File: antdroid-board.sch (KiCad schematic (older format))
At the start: 55 parts, among them P1 CONN_01X02, Q1 BSS138, Q2 BSS138, U1 LM2678T-5.0, U2 LM2678T-5.0, U3 LM2675M-5

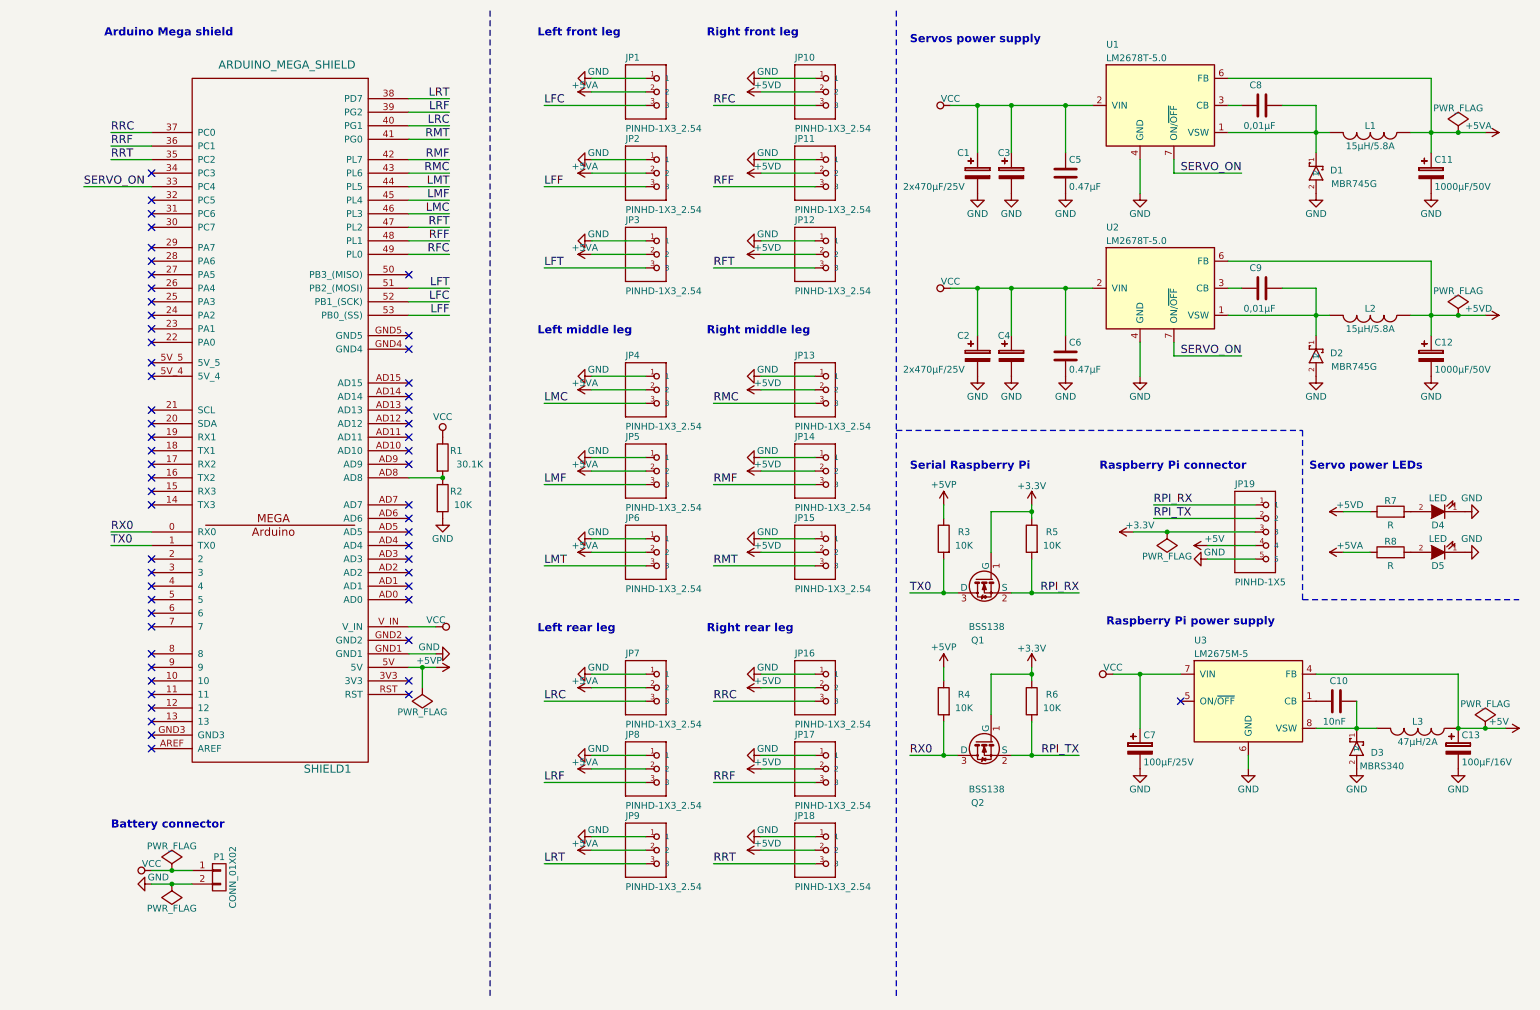
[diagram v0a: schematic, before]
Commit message: All components positioned and design rules almost done
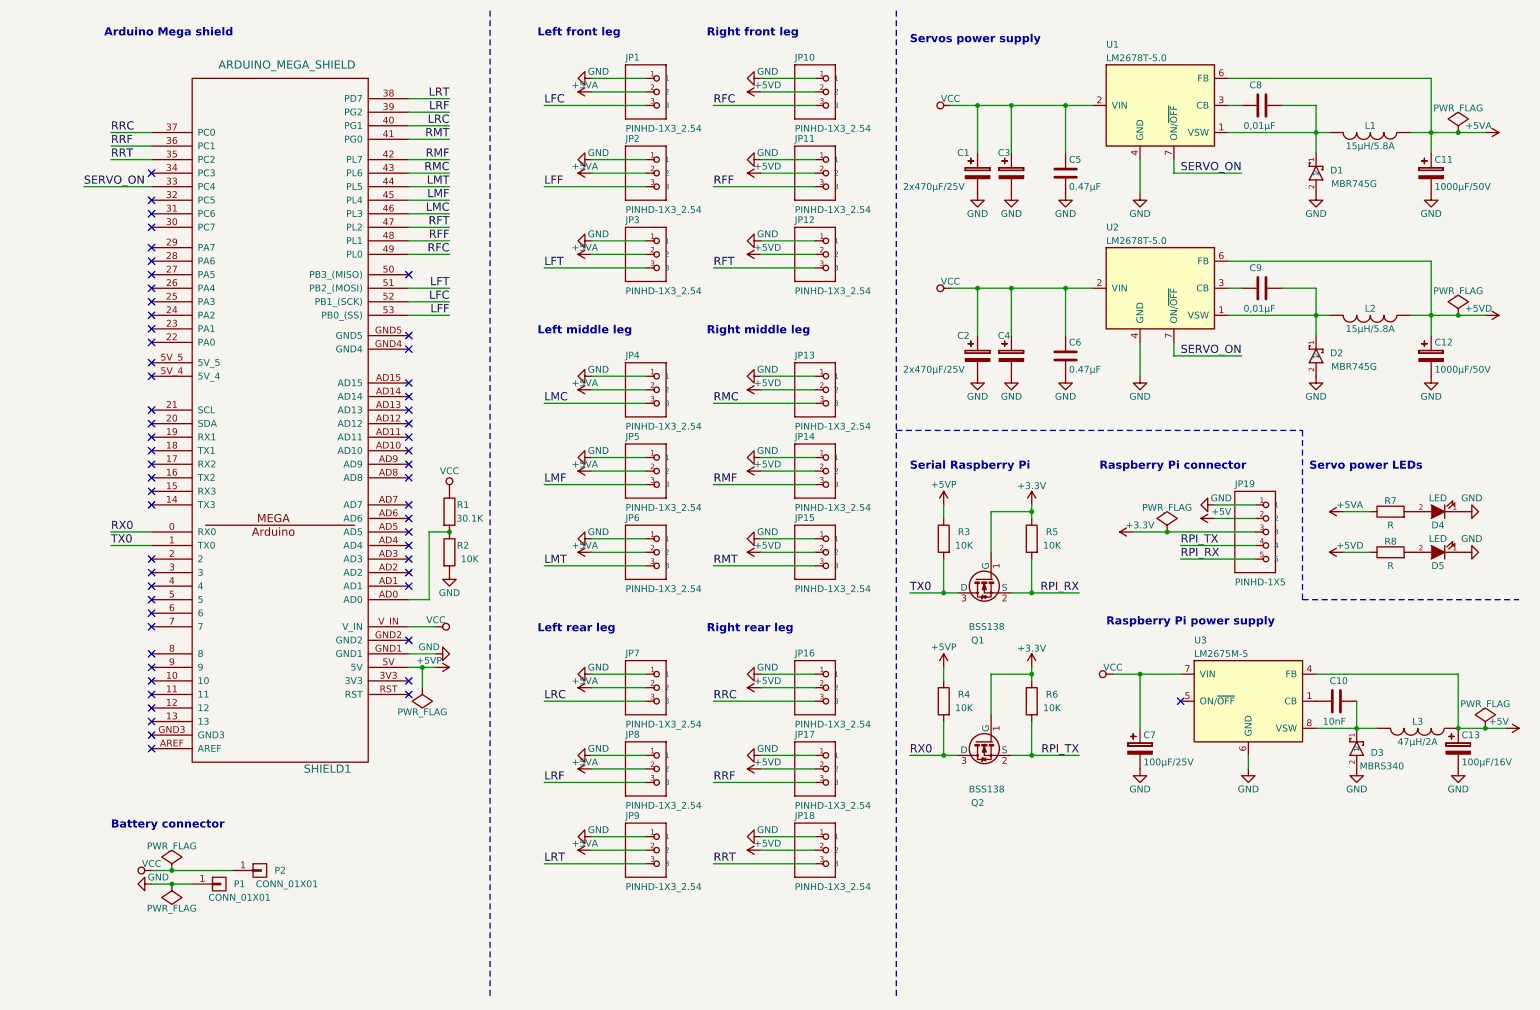
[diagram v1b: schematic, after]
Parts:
- removed P1: CONN_01X02, Connect:AK300-2, symbol CONN_01X02
- added P1, P2: CONN_01X01, Connect:1pin, symbol CONN_01X01
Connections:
- net +5V: now also JP19.2; no longer JP19.4
- net +5VA: now also R7.1; no longer R8.1
- net +5VD: now also R8.1; no longer R7.1
- net GND: now also JP19.1, P1.1 (P1); no longer JP19.5
- net RPI_RX: now also JP19.5; no longer JP19.1
- net RPI_TX: now also JP19.4; no longer JP19.2
- net VCC: now also P2.1 (P1)
- net at SHIELD1.AD0: now also R1.2, R2.1
- now unconnected: SHIELD1.AD8
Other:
- moved on the sheet: R1, R2
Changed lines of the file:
@@
 LIBS:device
 LIBS:pinhead
-LIBS:pinhead-1
 LIBS:led
 LIBS:led_rgb
@@
 NoConn ~ 3000 4650
 NoConn ~ 3000 4750
-NoConn ~ 3000 4850
+NoConn ~ 3000 3950
 NoConn ~ 3000 5450
 NoConn ~ 3000 5550
@@
 	0    -1   -1   0
 $EndComp
-$Comp
-L CONN_01X02 P1
-U 1 1 559DC5EE
-P 1600 6900
-F 0 "P1" H 1600 7050 50  0000 C CNN
-F 1 "CONN_01X02" V 1700 6900 50  0000 C CNN
-F 2 "Connect:AK300-2" H 1600 6900 60  0001 C CNN
-F 3 "http://futurlec.com/Connectors/PCBT2.shtml" H 1600 6900 60  0001 C CNN
-	1    1600 6900
-	1    0    0    -1
-$EndComp
 Text Notes 800  6550 0    60   ~ 12
 Battery connector
@@
 Text Label 600  1800 0    60   ~ 0
 SERVO_ON
-Text Label 8500 4150 0    60   ~ 0
+Text Label 8700 4550 0    60   ~ 0
 RPI_RX
-Text Label 8500 4250 0    60   ~ 0
+Text Label 8700 4450 0    60   ~ 0
 RPI_TX
 Text Notes 8100 3900 0    60   ~ 12
@@
 L GND #PWR043
 U 1 1 55A01E1A
-P 8900 4550
-F 0 "#PWR043" H 8900 4300 50  0001 C CNN
-F 1 "GND" V 8850 4600 50  0000 C CNN
-F 2 "" H 8900 4550 60  0000 C CNN
-F 3 "" H 8900 4550 60  0000 C CNN
-	1    8900 4550
+P 8950 4150
+F 0 "#PWR043" H 8950 3900 50  0001 C CNN
+F 1 "GND" V 8900 4200 50  0000 C CNN
+F 2 "" H 8950 4150 60  0000 C CNN
+F 3 "" H 8950 4150 60  0000 C CNN
+	1    8950 4150
 	0    1    1    0
 $EndComp
@@
 F 3 "" H 8600 4350 60  0000 C CNN
 	1    8600 4350
-	-1   0    0    1
+	1    0    0    -1
 $EndComp
 Wire Wire Line
@@
 	8350 4350 9250 4350
 Wire Wire Line
-	8500 4150 9250 4150
-Wire Wire Line
-	8500 4250 9250 4250
-Wire Wire Line
-	9250 4450 8900 4450
-Wire Wire Line
-	9250 4550 8900 4550
+	8950 4150 9250 4150
+Wire Wire Line
+	8950 4250 9250 4250
+Wire Wire Line
+	9250 4450 8700 4450
+Wire Wire Line
+	9250 4550 8700 4550
 Connection ~ 8600 4350
 Wire Wire Line
@@
 Connection ~ 1250 6850
 Wire Wire Line
-	1100 6850 1400 6850
+	1100 6850 1700 6850
 $Comp
 L PWR_FLAG #FLG045
@@
 L R R2
 U 1 1 559DDEEC
-P 3250 4100
-F 0 "R2" H 3350 4150 50  0000 C CNN
-F 1 "10K" H 3400 4050 50  0000 C CNN
-F 2 "Resistors_SMD:R_0603_HandSoldering" V 3180 4100 30  0001 C CNN
-F 3 "" H 3250 4100 30  0000 C CNN
-	1    3250 4100
+P 3300 4500
+F 0 "R2" H 3400 4550 50  0000 C CNN
+F 1 "10K" H 3450 4450 50  0000 C CNN
+F 2 "Resistors_SMD:R_0603_HandSoldering" V 3230 4500 30  0001 C CNN
+F 3 "" H 3300 4500 30  0000 C CNN
+	1    3300 4500
 	1    0    0    -1
 $EndComp
@@
 L R R1
 U 1 1 559DDFF3
-P 3250 3800
-F 0 "R1" H 3350 3850 50  0000 C CNN
-F 1 "30.1K" H 3450 3750 50  0000 C CNN
-F 2 "Resistors_SMD:R_0603_HandSoldering" V 3180 3800 30  0001 C CNN
-F 3 "" H 3250 3800 30  0000 C CNN
-	1    3250 3800
+P 3300 4200
+F 0 "R1" H 3400 4250 50  0000 C CNN
+F 1 "30.1K" H 3450 4150 50  0000 C CNN
+F 2 "Resistors_SMD:R_0603_HandSoldering" V 3230 4200 30  0001 C CNN
+F 3 "" H 3300 4200 30  0000 C CNN
+	1    3300 4200
 	1    0    0    -1
 $EndComp
@@
 L VCC #PWR047
 U 1 1 559DE0A4
-P 3250 3650
-F 0 "#PWR047" H 3250 3500 50  0001 C CNN
-F 1 "VCC" H 3250 3800 50  0000 C CNN
-F 2 "" H 3250 3650 60  0000 C CNN
-F 3 "" H 3250 3650 60  0000 C CNN
-	1    3250 3650
+P 3300 4050
+F 0 "#PWR047" H 3300 3900 50  0001 C CNN
+F 1 "VCC" H 3300 4200 50  0000 C CNN
+F 2 "" H 3300 4050 60  0000 C CNN
+F 3 "" H 3300 4050 60  0000 C CNN
+	1    3300 4050
 	1    0    0    -1
 $EndComp
@@
 L GND #PWR048
 U 1 1 559DE122
-P 3250 4250
-F 0 "#PWR048" H 3250 4000 50  0001 C CNN
-F 1 "GND" H 3250 4100 50  0000 C CNN
-F 2 "" H 3250 4250 60  0000 C CNN
-F 3 "" H 3250 4250 60  0000 C CNN
-	1    3250 4250
-	1    0    0    -1
-$EndComp
-Wire Wire Line
-	3250 3950 3000 3950
-Connection ~ 3250 3950
+P 3300 4650
+F 0 "#PWR048" H 3300 4400 50  0001 C CNN
+F 1 "GND" H 3300 4500 50  0000 C CNN
+F 2 "" H 3300 4650 60  0000 C CNN
+F 3 "" H 3300 4650 60  0000 C CNN
+	1    3300 4650
+	1    0    0    -1
+$EndComp
+Wire Wire Line
+	3300 4350 3150 4350
+Connection ~ 3300 4350
 $Comp
 L +5VA #PWR049
@@
 L +5VD #PWR074
 U 1 1 559FE79D
-P 9900 4200
-F 0 "#PWR074" H 9900 4050 50  0001 C CNN
-F 1 "+5VD" V 9950 4150 50  0000 C CNN
-F 2 "" H 9900 4200 60  0000 C CNN
-F 3 "" H 9900 4200 60  0000 C CNN
-	1    9900 4200
+P 9900 4500
+F 0 "#PWR074" H 9900 4350 50  0001 C CNN
+F 1 "+5VD" V 9950 4450 50  0000 C CNN
+F 2 "" H 9900 4500 60  0000 C CNN
+F 3 "" H 9900 4500 60  0000 C CNN
+	1    9900 4500
 	0    -1   -1   0
 $EndComp
@@
 L +5VA #PWR076
 U 1 1 559FEA9D
-P 9900 4500
-F 0 "#PWR076" H 9900 4350 50  0001 C CNN
-F 1 "+5VA" V 9950 4450 50  0000 C CNN
-F 2 "" H 9900 4500 60  0000 C CNN
-F 3 "" H 9900 4500 60  0000 C CNN
-	1    9900 4500
+P 9900 4200
+F 0 "#PWR076" H 9900 4050 50  0001 C CNN
+F 1 "+5VA" V 9950 4150 50  0000 C CNN
+F 2 "" H 9900 4200 60  0000 C CNN
+F 3 "" H 9900 4200 60  0000 C CNN
+	1    9900 4200
 	0    -1   -1   0
 $EndComp
@@
 L +5V #PWR079
 U 1 1 55A0450F
-P 8900 4450
-F 0 "#PWR079" H 8900 4300 50  0001 C CNN
-F 1 "+5V" V 8950 4400 50  0000 C CNN
-F 2 "" H 8900 4450 60  0000 C CNN
-F 3 "" H 8900 4450 60  0000 C CNN
-	1    8900 4450
+P 8950 4250
+F 0 "#PWR079" H 8950 4100 50  0001 C CNN
+F 1 "+5V" V 9000 4200 50  0000 C CNN
+F 2 "" H 8950 4250 60  0000 C CNN
+F 3 "" H 8950 4250 60  0000 C CNN
+	1    8950 4250
 	0    -1   -1   0
 $EndComp
@@
 Arduino Mega shield
 Connection ~ 10000 5800
+$Comp
+L CONN_01X01 P2
+U 1 1 55A11992
+P 1900 6850
+F 0 "P2" H 2050 6850 50  0000 C CNN
+F 1 "CONN_01X01" H 2100 6750 50  0000 C CNN
+F 2 "Connect:1pin" H 1900 6850 60  0001 C CNN
+F 3 "" H 1900 6850 60  0000 C CNN
+	1    1900 6850
+	1    0    0    -1
+$EndComp
+$Comp
+L CONN_01X01 P1
+U 1 1 55A11AAA
+P 1600 6950
+F 0 "P1" H 1750 6950 50  0000 C CNN
+F 1 "CONN_01X01" H 1750 6850 50  0000 C CNN
+F 2 "Connect:1pin" H 1600 6950 60  0001 C CNN
+F 3 "" H 1600 6950 60  0000 C CNN
+	1    1600 6950
+	1    0    0    -1
+$EndComp
+Wire Wire Line
+	3150 4350 3150 4850
+Wire Wire Line
+	3150 4850 3000 4850
 $EndSCHEMATC

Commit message: Adding edges
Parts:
- SHIELD1: footprint arduino_shields:ARDUINO MEGA SHIELD -> antdroid-board:ARDUINO MEGA SHIELD
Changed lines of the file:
@@
 F 0 "SHIELD1" H 1600 6100 60  0000 C CNN
 F 1 "ARDUINO_MEGA_SHIELD" H 1900 900 60  0000 C CNN
-F 2 "arduino_shields:ARDUINO MEGA SHIELD" H 2000 3600 60  0001 C CNN
+F 2 "antdroid-board:ARDUINO MEGA SHIELD" H 2000 3600 60  0001 C CNN
 F 3 "" H 2000 3600 60  0000 C CNN
 	1    2000 3600

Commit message: Almost tracked and logo added
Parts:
- SHIELD1: footprint antdroid-board:ARDUINO MEGA SHIELD -> antdroid-board:ArduinoMegaShield
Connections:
- net +5VP: now also SHIELD1.5V_4; no longer SHIELD1.5V
- net GND: now also SHIELD1.GND2, SHIELD1.GND3, SHIELD1.GND4, SHIELD1.GND5
- no-connect marks 58 -> 54
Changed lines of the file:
@@
 F 0 "SHIELD1" H 1600 6100 60  0000 C CNN
 F 1 "ARDUINO_MEGA_SHIELD" H 1900 900 60  0000 C CNN
-F 2 "antdroid-board:ARDUINO MEGA SHIELD" H 2000 3600 60  0001 C CNN
+F 2 "antdroid-board:ArduinoMegaShield" H 2000 3600 60  0001 C CNN
 F 3 "" H 2000 3600 60  0000 C CNN
 	1    2000 3600
@@
 L GND #PWR013
 U 1 1 559E57B9
-P 3200 5250
-F 0 "#PWR013" H 3200 5000 50  0001 C CNN
-F 1 "GND" V 3250 5300 50  0000 C CNN
-F 2 "" H 3200 5250 60  0000 C CNN
-F 3 "" H 3200 5250 60  0000 C CNN
-	1    3200 5250
-	0    -1   -1   0
-$EndComp
-NoConn ~ 3000 5150
+P 3150 5200
+F 0 "#PWR013" H 3150 4950 50  0001 C CNN
+F 1 "GND" V 3200 5250 50  0000 C CNN
+F 2 "" H 3150 5200 60  0000 C CNN
+F 3 "" H 3150 5200 60  0000 C CNN
+	1    3150 5200
+	0    -1   -1   0
+$EndComp
 Text Notes 9650 3900 0    60   ~ 12
 Servo power LEDs
@@
 Text Label 800  1600 0    60   ~ 0
 RRT
-NoConn ~ 3000 2900
-NoConn ~ 3000 3000
 NoConn ~ 3000 3250
 NoConn ~ 3000 3350
@@
 NoConn ~ 3000 5550
 NoConn ~ 1100 5950
-NoConn ~ 1100 5850
 NoConn ~ 1100 5750
 NoConn ~ 1100 5650
@@
 NoConn ~ 1100 3550
 NoConn ~ 1100 3450
-NoConn ~ 1100 3200
-NoConn ~ 1100 3100
 NoConn ~ 1100 2950
 NoConn ~ 1100 2850
@@
 	3200 5050 3000 5050
 Wire Wire Line
-	3200 5250 3000 5250
-Wire Wire Line
 	1100 4350 800  4350
 Wire Wire Line
@@
 $EndComp
 $Comp
-L +5VP #PWR080
-U 1 1 55A09371
-P 3200 5350
-F 0 "#PWR080" H 3200 5200 50  0001 C CNN
-F 1 "+5VP" V 3150 5300 50  0000 C CNN
-F 2 "" H 3200 5350 60  0000 C CNN
-F 3 "" H 3200 5350 60  0000 C CNN
-	1    3200 5350
-	0    1    1    0
-$EndComp
-Wire Wire Line
-	3000 5350 3200 5350
-$Comp
 L PWR_FLAG #FLG081
 U 1 1 55A099EC
-P 3100 5500
-F 0 "#FLG081" H 3100 5595 50  0001 C CNN
-F 1 "PWR_FLAG" H 3100 5680 50  0000 C CNN
-F 2 "" H 3100 5500 60  0000 C CNN
-F 3 "" H 3100 5500 60  0000 C CNN
-	1    3100 5500
+P 850 3300
+F 0 "#FLG081" H 850 3395 50  0001 C CNN
+F 1 "PWR_FLAG" H 850 3480 50  0000 C CNN
+F 2 "" H 850 3300 60  0000 C CNN
+F 3 "" H 850 3300 60  0000 C CNN
+	1    850  3300
 	-1   0    0    1
 $EndComp
-Wire Wire Line
-	3100 5500 3100 5350
-Connection ~ 3100 5350
 $Comp
 L +5VP #PWR082
@@
 Wire Wire Line
 	3150 4850 3000 4850
+$Comp
+L GND #PWR084
+U 1 1 55A26536
+P 3150 2950
+F 0 "#PWR084" H 3150 2700 50  0001 C CNN
+F 1 "GND" V 3200 3000 50  0000 C CNN
+F 2 "" H 3150 2950 60  0000 C CNN
+F 3 "" H 3150 2950 60  0000 C CNN
+	1    3150 2950
+	0    -1   -1   0
+$EndComp
+Wire Wire Line
+	3000 2900 3000 3000
+Wire Wire Line
+	3150 2950 3000 2950
+Connection ~ 3000 2950
+$Comp
+L GND #PWR085
+U 1 1 55A26A0D
+P 950 5850
+F 0 "#PWR085" H 950 5600 50  0001 C CNN
+F 1 "GND" V 900 5900 50  0000 C CNN
+F 2 "" H 950 5850 60  0000 C CNN
+F 3 "" H 950 5850 60  0000 C CNN
+	1    950  5850
+	0    1    1    0
+$EndComp
+Wire Wire Line
+	1100 5850 950  5850
+Wire Wire Line
+	3000 5150 3000 5250
+Wire Wire Line
+	3150 5200 3000 5200
+Connection ~ 3000 5200
+$Comp
+L +5VP #PWR086
+U 1 1 55A2A2AB
+P 750 3200
+F 0 "#PWR086" H 750 3050 50  0001 C CNN
+F 1 "+5VP" V 800 3150 50  0000 C CNN
+F 2 "" H 750 3200 60  0000 C CNN
+F 3 "" H 750 3200 60  0000 C CNN
+	1    750  3200
+	0    -1   -1   0
+$EndComp
+NoConn ~ 1100 3100
+Wire Wire Line
+	1100 3200 750  3200
+NoConn ~ 3000 5350
+Wire Wire Line
+	850  3300 850  3200
+Connection ~ 850  3200
 $EndSCHEMATC
